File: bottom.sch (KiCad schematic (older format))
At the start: 8 parts, among them J6 FFC-0.5MM-6POS, J7 Conn_01x02, J8 Conn_01x02

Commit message: Move BNC connectors to correct hemispheres
Positions within the hemisphere don’t matter.
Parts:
- J7: value Conn_01x02 -> Port_3
- J8: value Conn_01x02 -> Port_4
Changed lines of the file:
@@
 P 3500 1000
 F 0 "J7" H 3580 992 50  0000 L CNN
-F 1 "Conn_01x02" H 3580 901 50  0000 L CNN
+F 1 "Port_3" H 3580 901 50  0000 L CNN
 F 2 "Connector_PinHeader_1.27mm:PinHeader_1x02_P1.27mm_Vertical" H 3500 1000 50  0001 C CNN
 F 3 "~" H 3500 1000 50  0001 C CNN
@@
 P 3500 1500
 F 0 "J8" H 3580 1492 50  0000 L CNN
-F 1 "Conn_01x02" H 3580 1401 50  0000 L CNN
+F 1 "Port_4" H 3580 1401 50  0000 L CNN
 F 2 "Connector_PinHeader_1.27mm:PinHeader_1x02_P1.27mm_Vertical" H 3500 1500 50  0001 C CNN
 F 3 "~" H 3500 1500 50  0001 C CNN

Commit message: Changed to 2.54mm
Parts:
- D4, D5: footprint Connector_PinHeader_1.27mm:PinHeader_1x04_P1.27mm_Vertical -> Connector_PinHeader_2.54mm:PinHeader_1x04_P2.54mm_Vertical
- J7, J8: footprint Connector_PinHeader_1.27mm:PinHeader_1x02_P1.27mm_Vertical -> Connector_PinHeader_2.54mm:PinHeader_1x02_P2.54mm_Vertical
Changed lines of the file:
@@
 F 0 "J7" H 3580 992 50  0000 L CNN
 F 1 "Port_3" H 3580 901 50  0000 L CNN
-F 2 "Connector_PinHeader_1.27mm:PinHeader_1x02_P1.27mm_Vertical" H 3500 1000 50  0001 C CNN
+F 2 "Connector_PinHeader_2.54mm:PinHeader_1x02_P2.54mm_Vertical" H 3500 1000 50  0001 C CNN
 F 3 "~" H 3500 1000 50  0001 C CNN
 	1    3500 1000
@@
 F 0 "J8" H 3580 1492 50  0000 L CNN
 F 1 "Port_4" H 3580 1401 50  0000 L CNN
-F 2 "Connector_PinHeader_1.27mm:PinHeader_1x02_P1.27mm_Vertical" H 3500 1500 50  0001 C CNN
+F 2 "Connector_PinHeader_2.54mm:PinHeader_1x02_P2.54mm_Vertical" H 3500 1500 50  0001 C CNN
 F 3 "~" H 3500 1500 50  0001 C CNN
 	1    3500 1500
@@
 F 0 "D5" H 4100 2850 50  0000 L CNN
 F 1 "NeoPixel_THT" H 4350 2350 50  0000 L CNN
-F 2 "Connector_PinHeader_1.27mm:PinHeader_1x04_P1.27mm_Vertical" H 4350 2300 50  0001 L TNN
+F 2 "Connector_PinHeader_2.54mm:PinHeader_1x04_P2.54mm_Vertical" H 4350 2300 50  0001 L TNN
 F 3 "https://www.adafruit.com/product/1938" H 4400 2225 50  0001 L TNN
 F 4 "1938" H 0   0   50  0001 C CNN "MPN"
@@
 F 0 "D4" H 3150 2850 50  0000 L CNN
 F 1 "NeoPixel_THT" H 3400 2350 50  0000 L CNN
-F 2 "Connector_PinHeader_1.27mm:PinHeader_1x04_P1.27mm_Vertical" H 3400 2300 50  0001 L TNN
+F 2 "Connector_PinHeader_2.54mm:PinHeader_1x04_P2.54mm_Vertical" H 3400 2300 50  0001 L TNN
 F 3 "https://www.adafruit.com/product/1938" H 3450 2225 50  0001 L TNN
 F 4 "1938" H 0   0   50  0001 C CNN "MPN"

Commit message: Numbered LEDs (values)
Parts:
- D4: value NeoPixel_THT -> LED 3
- D5: value NeoPixel_THT -> LED 4
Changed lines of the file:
@@
 AR Path="/5C99B5FE" Ref="BT?"  Part="1"
 AR Path="/5C920CA4/5C99B5FE" Ref="BT2"  Part="1"
-F 0 "BT2" H 1918 2546 50  0000 L CNN
+F 0 "BT?" H 1918 2546 50  0000 L CNN
 F 1 "CR2032" H 1918 2455 50  0000 L CNN
 F 2 "gsg-modules:BK-912" V 1800 2510 50  0001 C CNN
@@
 U 1 1 5CA58E18
 P 1800 2550
-F 0 "#PWR033" H 1800 2300 50  0001 C CNN
+F 0 "#PWR?" H 1800 2300 50  0001 C CNN
 F 1 "GND" H 1805 2377 50  0000 C CNN
 F 2 "" H 1800 2550 50  0001 C CNN
@@
 U 1 1 5CA5A9D9
 P 3500 1000
-F 0 "J7" H 3580 992 50  0000 L CNN
+F 0 "J?" H 3580 992 50  0000 L CNN
 F 1 "Port_3" H 3580 901 50  0000 L CNN
 F 2 "Connector_PinHeader_2.54mm:PinHeader_1x02_P2.54mm_Vertical" H 3500 1000 50  0001 C CNN
@@
 U 1 1 5CA5ADA9
 P 3500 1500
-F 0 "J8" H 3580 1492 50  0000 L CNN
+F 0 "J?" H 3580 1492 50  0000 L CNN
 F 1 "Port_4" H 3580 1401 50  0000 L CNN
 F 2 "Connector_PinHeader_2.54mm:PinHeader_1x02_P2.54mm_Vertical" H 3500 1500 50  0001 C CNN
@@
 U 1 1 5CA792A5
 P 1850 1600
-F 0 "#PWR034" H 1850 1350 50  0001 C CNN
+F 0 "#PWR?" H 1850 1350 50  0001 C CNN
 F 1 "GND" H 1855 1427 50  0000 C CNN
 F 2 "" H 1850 1600 50  0001 C CNN
@@
 U 1 1 5CA79E38
 P 1450 950
-F 0 "#PWR032" H 1450 800 50  0001 C CNN
+F 0 "#PWR?" H 1450 800 50  0001 C CNN
 F 1 "+5V" H 1465 1123 50  0000 C CNN
 F 2 "" H 1450 950 50  0001 C CNN
@@
 U 1 1 5CA7C65D
 P 1100 1350
-F 0 "J6" H 1100 950 50  0000 C CNN
+F 0 "J?" H 1100 950 50  0000 C CNN
 F 1 "FFC-0.5MM-6POS" H 1250 1700 50  0000 C CNN
 F 2 "Connector_FFC-FPC:Hirose_FH12-6S-0.5SH_1x06-1MP_P0.50mm_Horizontal" H 1100 1350 50  0001 C CNN
@@
 U 1 1 5CA7ED40
 P 3300 1600
-F 0 "#PWR036" H 3300 1350 50  0001 C CNN
+F 0 "#PWR?" H 3300 1350 50  0001 C CNN
 F 1 "GND" H 3305 1427 50  0000 C CNN
 F 2 "" H 3300 1600 50  0001 C CNN
@@
 U 1 1 5CA7F049
 P 3300 1100
-F 0 "#PWR035" H 3300 850 50  0001 C CNN
+F 0 "#PWR?" H 3300 850 50  0001 C CNN
 F 1 "GND" H 3305 927 50  0000 C CNN
 F 2 "" H 3300 1100 50  0001 C CNN
@@
 AR Path="/5C920754/5CA85CAB" Ref="#PWR?"  Part="1"
 AR Path="/5C920CA4/5CA85CAB" Ref="#PWR037"  Part="1"
-F 0 "#PWR037" H 3350 2000 50  0001 C CNN
+F 0 "#PWR?" H 3350 2000 50  0001 C CNN
 F 1 "+5V" H 3365 2323 50  0000 C CNN
 F 2 "" H 3350 2150 50  0001 C CNN
@@
 AR Path="/5C920754/5CA85CB1" Ref="#PWR?"  Part="1"
 AR Path="/5C920CA4/5CA85CB1" Ref="#PWR039"  Part="1"
-F 0 "#PWR039" H 4300 2000 50  0001 C CNN
+F 0 "#PWR?" H 4300 2000 50  0001 C CNN
 F 1 "+5V" H 4315 2323 50  0000 C CNN
 F 2 "" H 4300 2150 50  0001 C CNN
@@
 AR Path="/5C920754/5CA85CB7" Ref="C?"  Part="1"
 AR Path="/5C920CA4/5CA85CB7" Ref="C12"  Part="1"
-F 0 "C12" H 3792 2396 50  0000 L CNN
+F 0 "C?" H 3792 2396 50  0000 L CNN
 F 1 "0.1u" H 3792 2305 50  0000 L CNN
 F 2 "Capacitor_SMD:C_0402_1005Metric" H 3700 2350 50  0001 C CNN
@@
 AR Path="/5C920754/5CA85CBD" Ref="C?"  Part="1"
 AR Path="/5C920CA4/5CA85CBD" Ref="C13"  Part="1"
-F 0 "C13" H 4742 2396 50  0000 L CNN
+F 0 "C?" H 4742 2396 50  0000 L CNN
 F 1 "0.1u" H 4742 2305 50  0000 L CNN
 F 2 "Capacitor_SMD:C_0402_1005Metric" H 4650 2350 50  0001 C CNN
@@
 AR Path="/5C920754/5CA85CC5" Ref="#PWR?"  Part="1"
 AR Path="/5C920CA4/5CA85CC5" Ref="#PWR040"  Part="1"
-F 0 "#PWR040" H 4300 2750 50  0001 C CNN
+F 0 "#PWR?" H 4300 2750 50  0001 C CNN
 F 1 "GND" H 4305 2827 50  0000 C CNN
 F 2 "" H 4300 3000 50  0001 C CNN
@@
 AR Path="/5C920754/5CA85CCB" Ref="#PWR?"  Part="1"
 AR Path="/5C920CA4/5CA85CCB" Ref="#PWR038"  Part="1"
-F 0 "#PWR038" H 3350 2750 50  0001 C CNN
+F 0 "#PWR?" H 3350 2750 50  0001 C CNN
 F 1 "GND" H 3355 2827 50  0000 C CNN
 F 2 "" H 3350 3000 50  0001 C CNN
@@
 AR Path="/5C920754/5CA85CD2" Ref="D?"  Part="1"
 AR Path="/5C920CA4/5CA85CD2" Ref="D5"  Part="1"
-F 0 "D5" H 4100 2850 50  0000 L CNN
-F 1 "NeoPixel_THT" H 4350 2350 50  0000 L CNN
+F 0 "D?" H 4100 2850 50  0000 L CNN
+F 1 "LED 4" H 4350 2350 50  0000 L CNN
 F 2 "Connector_PinHeader_2.54mm:PinHeader_1x04_P2.54mm_Vertical" H 4350 2300 50  0001 L TNN
 F 3 "https://www.adafruit.com/product/1938" H 4400 2225 50  0001 L TNN
@@
 AR Path="/5C920754/5CA85CD8" Ref="D?"  Part="1"
 AR Path="/5C920CA4/5CA85CD8" Ref="D4"  Part="1"
-F 0 "D4" H 3150 2850 50  0000 L CNN
-F 1 "NeoPixel_THT" H 3400 2350 50  0000 L CNN
+F 0 "D?" H 3150 2850 50  0000 L CNN
+F 1 "LED 3" H 3400 2350 50  0000 L CNN
 F 2 "Connector_PinHeader_2.54mm:PinHeader_1x04_P2.54mm_Vertical" H 3400 2300 50  0001 L TNN
 F 3 "https://www.adafruit.com/product/1938" H 3450 2225 50  0001 L TNN

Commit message: Connect USB-Mini shield to GND
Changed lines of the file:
@@
 AR Path="/5C99B5FE" Ref="BT?"  Part="1"
 AR Path="/5C920CA4/5C99B5FE" Ref="BT2"  Part="1"
-F 0 "BT?" H 1918 2546 50  0000 L CNN
+F 0 "BT2" H 1918 2546 50  0000 L CNN
 F 1 "CR2032" H 1918 2455 50  0000 L CNN
 F 2 "gsg-modules:BK-912" V 1800 2510 50  0001 C CNN
@@
 GNDB
 $Comp
-L power:GND #PWR033
+L power:GND #PWR0101
 U 1 1 5CA58E18
 P 1800 2550
-F 0 "#PWR?" H 1800 2300 50  0001 C CNN
+F 0 "#PWR0101" H 1800 2300 50  0001 C CNN
 F 1 "GND" H 1805 2377 50  0000 C CNN
 F 2 "" H 1800 2550 50  0001 C CNN
@@
 U 1 1 5CA5A9D9
 P 3500 1000
-F 0 "J?" H 3580 992 50  0000 L CNN
+F 0 "J7" H 3580 992 50  0000 L CNN
 F 1 "Port_3" H 3580 901 50  0000 L CNN
 F 2 "Connector_PinHeader_2.54mm:PinHeader_1x02_P2.54mm_Vertical" H 3500 1000 50  0001 C CNN
@@
 U 1 1 5CA5ADA9
 P 3500 1500
-F 0 "J?" H 3580 1492 50  0000 L CNN
+F 0 "J8" H 3580 1492 50  0000 L CNN
 F 1 "Port_4" H 3580 1401 50  0000 L CNN
 F 2 "Connector_PinHeader_2.54mm:PinHeader_1x02_P2.54mm_Vertical" H 3500 1500 50  0001 C CNN
@@
 $EndComp
 $Comp
-L power:GND #PWR034
+L power:GND #PWR0102
 U 1 1 5CA792A5
 P 1850 1600
-F 0 "#PWR?" H 1850 1350 50  0001 C CNN
+F 0 "#PWR0102" H 1850 1350 50  0001 C CNN
 F 1 "GND" H 1855 1427 50  0000 C CNN
 F 2 "" H 1850 1600 50  0001 C CNN
@@
 	1850 1550 1950 1550
 $Comp
-L power:+5V #PWR032
+L power:+5V #PWR0103
 U 1 1 5CA79E38
 P 1450 950
-F 0 "#PWR?" H 1450 800 50  0001 C CNN
+F 0 "#PWR0103" H 1450 800 50  0001 C CNN
 F 1 "+5V" H 1465 1123 50  0000 C CNN
 F 2 "" H 1450 950 50  0001 C CNN
@@
 U 1 1 5CA7C65D
 P 1100 1350
-F 0 "J?" H 1100 950 50  0000 C CNN
+F 0 "J6" H 1100 950 50  0000 C CNN
 F 1 "FFC-0.5MM-6POS" H 1250 1700 50  0000 C CNN
 F 2 "Connector_FFC-FPC:Hirose_FH12-6S-0.5SH_1x06-1MP_P0.50mm_Horizontal" H 1100 1350 50  0001 C CNN
@@
 BNC-4
 $Comp
-L power:GND #PWR036
+L power:GND #PWR0104
 U 1 1 5CA7ED40
 P 3300 1600
-F 0 "#PWR?" H 3300 1350 50  0001 C CNN
+F 0 "#PWR0104" H 3300 1350 50  0001 C CNN
 F 1 "GND" H 3305 1427 50  0000 C CNN
 F 2 "" H 3300 1600 50  0001 C CNN
@@
 $EndComp
 $Comp
-L power:GND #PWR035
+L power:GND #PWR0105
 U 1 1 5CA7F049
 P 3300 1100
-F 0 "#PWR?" H 3300 850 50  0001 C CNN
+F 0 "#PWR0105" H 3300 850 50  0001 C CNN
 F 1 "GND" H 3305 927 50  0000 C CNN
 F 2 "" H 3300 1100 50  0001 C CNN
@@
 AR Path="/5C920754/5CA85CAB" Ref="#PWR?"  Part="1"
 AR Path="/5C920CA4/5CA85CAB" Ref="#PWR037"  Part="1"
-F 0 "#PWR?" H 3350 2000 50  0001 C CNN
+F 0 "#PWR037" H 3350 2000 50  0001 C CNN
 F 1 "+5V" H 3365 2323 50  0000 C CNN
 F 2 "" H 3350 2150 50  0001 C CNN
@@
 AR Path="/5C920754/5CA85CB1" Ref="#PWR?"  Part="1"
 AR Path="/5C920CA4/5CA85CB1" Ref="#PWR039"  Part="1"
-F 0 "#PWR?" H 4300 2000 50  0001 C CNN
+F 0 "#PWR039" H 4300 2000 50  0001 C CNN
 F 1 "+5V" H 4315 2323 50  0000 C CNN
 F 2 "" H 4300 2150 50  0001 C CNN
@@
 AR Path="/5C920754/5CA85CB7" Ref="C?"  Part="1"
 AR Path="/5C920CA4/5CA85CB7" Ref="C12"  Part="1"
-F 0 "C?" H 3792 2396 50  0000 L CNN
+F 0 "C12" H 3792 2396 50  0000 L CNN
 F 1 "0.1u" H 3792 2305 50  0000 L CNN
 F 2 "Capacitor_SMD:C_0402_1005Metric" H 3700 2350 50  0001 C CNN
@@
 AR Path="/5C920754/5CA85CBD" Ref="C?"  Part="1"
 AR Path="/5C920CA4/5CA85CBD" Ref="C13"  Part="1"
-F 0 "C?" H 4742 2396 50  0000 L CNN
+F 0 "C13" H 4742 2396 50  0000 L CNN
 F 1 "0.1u" H 4742 2305 50  0000 L CNN
 F 2 "Capacitor_SMD:C_0402_1005Metric" H 4650 2350 50  0001 C CNN
@@
 AR Path="/5C920754/5CA85CC5" Ref="#PWR?"  Part="1"
 AR Path="/5C920CA4/5CA85CC5" Ref="#PWR040"  Part="1"
-F 0 "#PWR?" H 4300 2750 50  0001 C CNN
+F 0 "#PWR040" H 4300 2750 50  0001 C CNN
 F 1 "GND" H 4305 2827 50  0000 C CNN
 F 2 "" H 4300 3000 50  0001 C CNN
@@
 AR Path="/5C920754/5CA85CCB" Ref="#PWR?"  Part="1"
 AR Path="/5C920CA4/5CA85CCB" Ref="#PWR038"  Part="1"
-F 0 "#PWR?" H 3350 2750 50  0001 C CNN
+F 0 "#PWR038" H 3350 2750 50  0001 C CNN
 F 1 "GND" H 3355 2827 50  0000 C CNN
 F 2 "" H 3350 3000 50  0001 C CNN
@@
 AR Path="/5C920754/5CA85CD2" Ref="D?"  Part="1"
 AR Path="/5C920CA4/5CA85CD2" Ref="D5"  Part="1"
-F 0 "D?" H 4100 2850 50  0000 L CNN
+F 0 "D5" H 4100 2850 50  0000 L CNN
 F 1 "LED 4" H 4350 2350 50  0000 L CNN
 F 2 "Connector_PinHeader_2.54mm:PinHeader_1x04_P2.54mm_Vertical" H 4350 2300 50  0001 L TNN
@@
 AR Path="/5C920754/5CA85CD8" Ref="D?"  Part="1"
 AR Path="/5C920CA4/5CA85CD8" Ref="D4"  Part="1"
-F 0 "D?" H 3150 2850 50  0000 L CNN
+F 0 "D4" H 3150 2850 50  0000 L CNN
 F 1 "LED 3" H 3400 2350 50  0000 L CNN
 F 2 "Connector_PinHeader_2.54mm:PinHeader_1x04_P2.54mm_Vertical" H 3400 2300 50  0001 L TNN

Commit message: Replace 2x1 header footprint by port footprint
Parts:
- J7, J8: footprint Connector_PinHeader_2.54mm:PinHeader_1x02_P2.54mm_Vertical -> node:port
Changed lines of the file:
@@
 F 0 "J7" H 3580 992 50  0000 L CNN
 F 1 "Port_3" H 3580 901 50  0000 L CNN
-F 2 "Connector_PinHeader_2.54mm:PinHeader_1x02_P2.54mm_Vertical" H 3500 1000 50  0001 C CNN
+F 2 "node:port" H 3500 1000 50  0001 C CNN
 F 3 "~" H 3500 1000 50  0001 C CNN
 	1    3500 1000
@@
 F 0 "J8" H 3580 1492 50  0000 L CNN
 F 1 "Port_4" H 3580 1401 50  0000 L CNN
-F 2 "Connector_PinHeader_2.54mm:PinHeader_1x02_P2.54mm_Vertical" H 3500 1500 50  0001 C CNN
+F 2 "node:port" H 3500 1500 50  0001 C CNN
 F 3 "~" H 3500 1500 50  0001 C CNN
 	1    3500 1500

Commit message: Switch to WS2812D-F5 footprints
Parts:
- D4, D5: footprint Connector_PinHeader_2.54mm:PinHeader_1x04_P2.54mm_Vertical -> node:WS2812D-F5
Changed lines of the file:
@@
 F 0 "D5" H 4100 2850 50  0000 L CNN
 F 1 "LED 4" H 4350 2350 50  0000 L CNN
-F 2 "Connector_PinHeader_2.54mm:PinHeader_1x04_P2.54mm_Vertical" H 4350 2300 50  0001 L TNN
+F 2 "node:WS2812D-F5" H 4350 2300 50  0001 L TNN
 F 3 "https://www.adafruit.com/product/1938" H 4400 2225 50  0001 L TNN
 F 4 "1938" H 0   0   50  0001 C CNN "MPN"
@@
 F 0 "D4" H 3150 2850 50  0000 L CNN
 F 1 "LED 3" H 3400 2350 50  0000 L CNN
-F 2 "Connector_PinHeader_2.54mm:PinHeader_1x04_P2.54mm_Vertical" H 3400 2300 50  0001 L TNN
+F 2 "node:WS2812D-F5" H 3400 2300 50  0001 L TNN
 F 3 "https://www.adafruit.com/product/1938" H 3450 2225 50  0001 L TNN
 F 4 "1938" H 0   0   50  0001 C CNN "MPN"

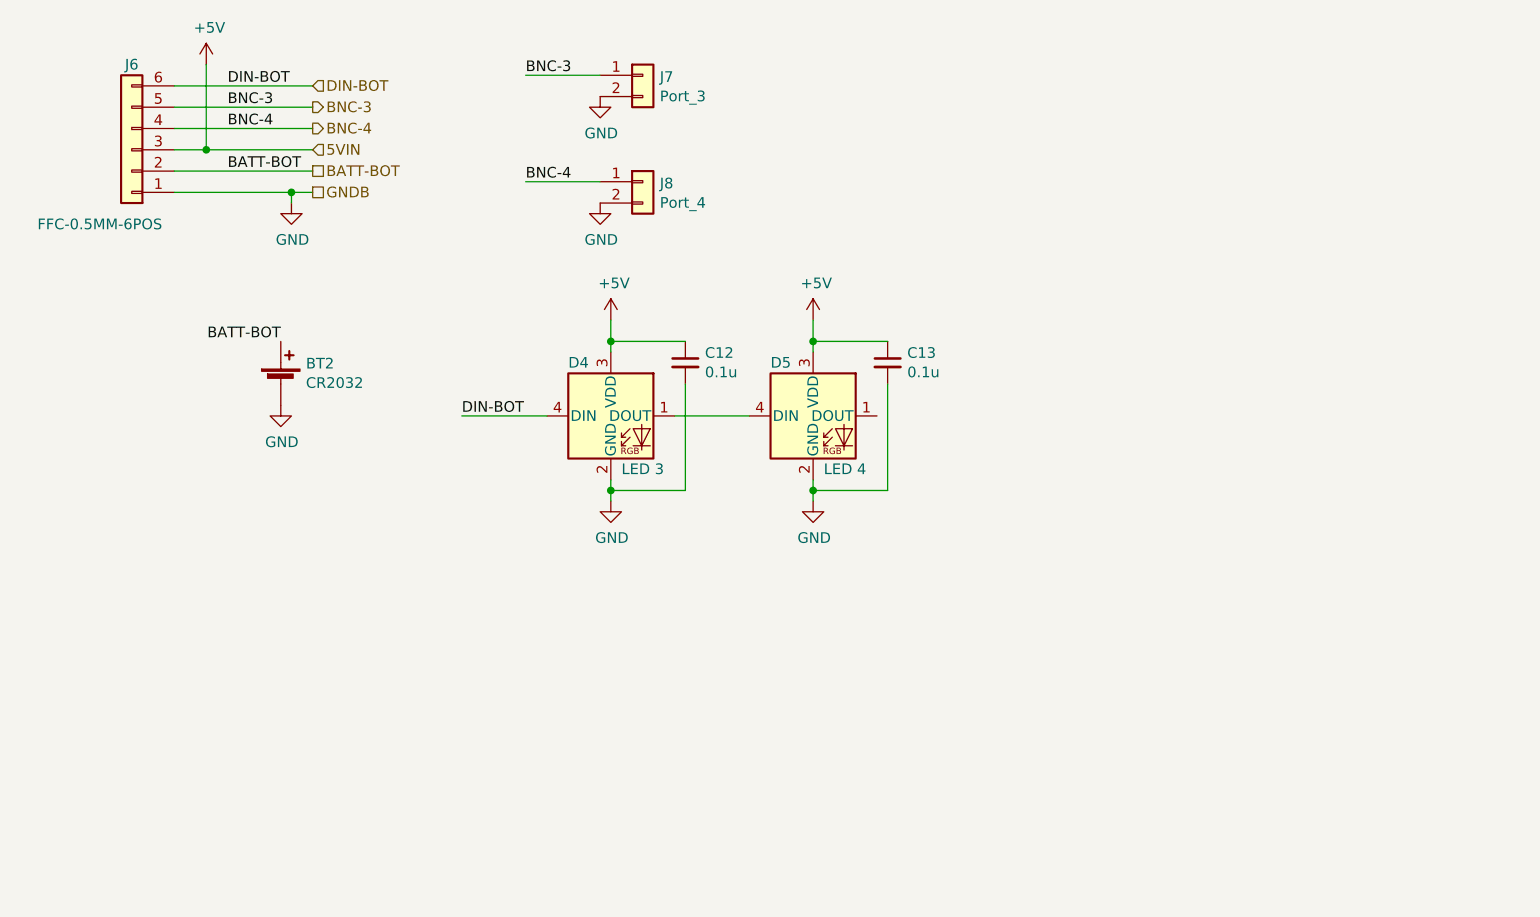
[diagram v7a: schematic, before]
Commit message: Switch to WS2812D-F5 (NeoPixel w/ diff. pinout)
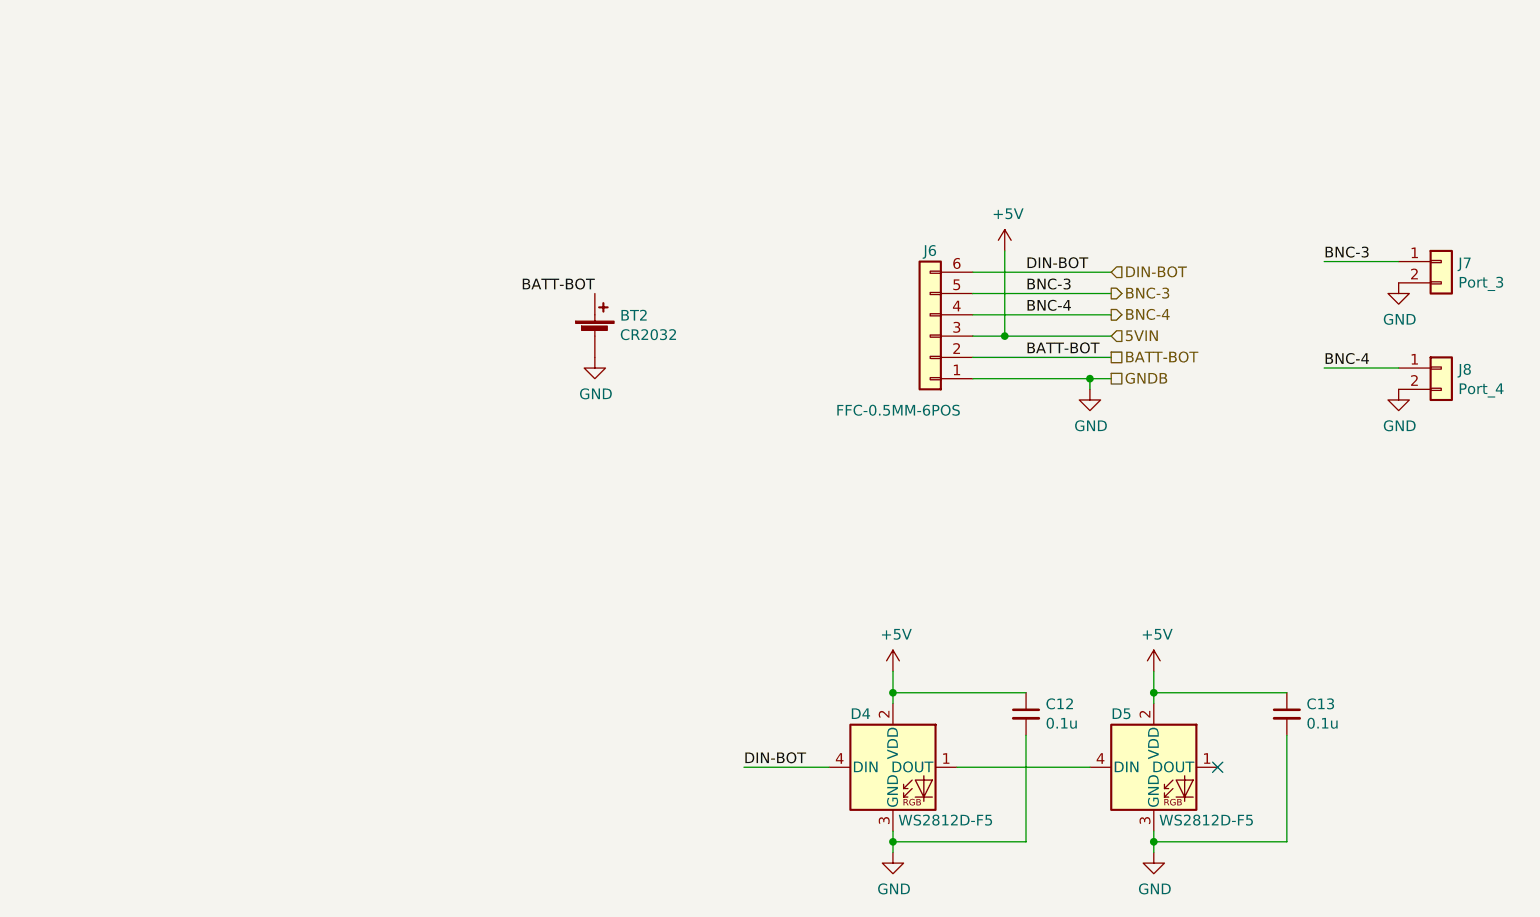
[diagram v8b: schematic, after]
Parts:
- removed D4: LED 3, node:WS2812D-F5, symbol LED:NeoPixel_THT
- removed D5: LED 4, node:WS2812D-F5, symbol LED:NeoPixel_THT
- added D4, D5: WS2812D-F5, node:WS2812D-F5, symbol node:WS2812D-F5
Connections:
- net +5V: now also D4.2 (VDD), D5.2 (VDD)
- net DIN-BOT: now also D4.4 (DIN)
- net GND: now also D4.3 (GND), D5.3 (GND)
- new net: D4.1 (DOUT), D5.4 (DIN)
- no-connect marks 0 -> 1
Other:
- moved on the sheet: BT2, C12, C13, J6, J7, J8
